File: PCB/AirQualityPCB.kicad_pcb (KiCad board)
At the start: 2 copper layers, 100 x 75 mm, 57 parts, among them J1 USB_C_Receptacle_USB2.0_16P, J10 SMA-J-P-H-ST-EM1, J2 TestPoint 5V, J3 TestPoint GND, J4 TestPoint 3.3V, U1 Regulator, U10 INIR2-ME5, U11 110-507, U12 110-303, U13 ESP32-C3-WROOM-02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

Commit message: Fixed op amp short bug
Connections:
- U7 pad 4: +3.3V -> GND
- U7 pad 8: GND -> +3.3V
- U8 pad 4: +3.3V -> GND
- U8 pad 8: GND -> +3.3V
- U9 pad 4: +3.3V -> GND
- U9 pad 8: GND -> +3.3V
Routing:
- net +3.3V: track 290.4 -> 333.6 mm
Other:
- board text added: "Air Quality Monitoring PCB MAE 5220 Designed by Robbie Leslie Cornell University School of Electrical and Computer Engineering School of Mechanical and Aerospace Engineering V1.1"
- board text removed: "Air Quality Monitoring PCB MAE 5220 Designed by Robbie Leslie Cornell University School of Electrical and Computer Engineering School of Mechanical and Aerospace Engineering"

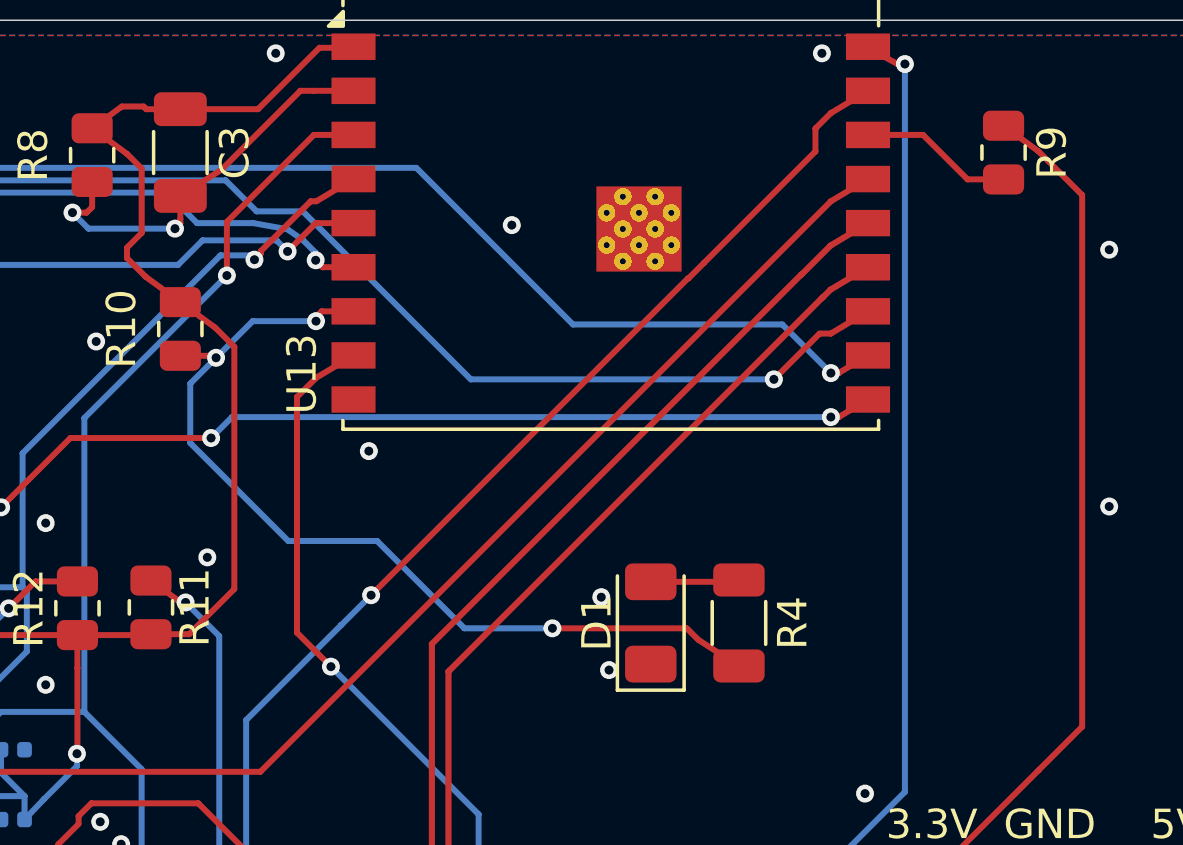
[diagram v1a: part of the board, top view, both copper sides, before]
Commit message: Swapped LED to pin 2
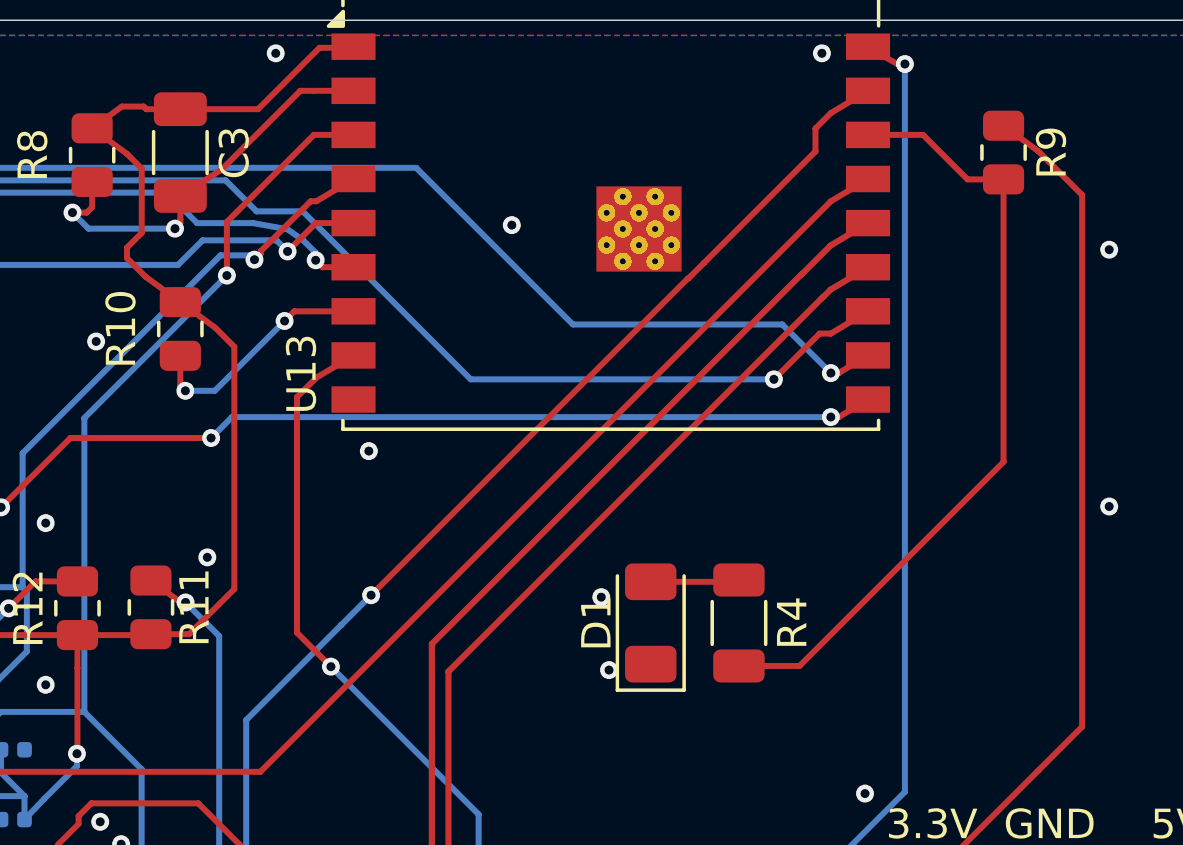
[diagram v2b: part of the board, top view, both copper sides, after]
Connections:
- R10 pad 2: /LED -> Net-(U13-IO8)
- R9 pad 2: Net-(U13-IO2) -> /LED
- U13 pad 16: Net-(U13-IO2) -> /LED
- U13 pad 7: /LED -> Net-(U13-IO8)
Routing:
- net Net-(U13-IO8): track 0.00 -> 8.28 mm, vias 0 -> 2
- net Net-(U13-IO2): track 5.24 -> 0.00 mm
- net /LED: track 31.6 -> 26.7 mm, vias 3 -> 0
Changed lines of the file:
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@@
 	(net 25 "/SDA")
 	(net 26 "Net-(U13-IO9)")
-	(net 27 "Net-(U13-IO2)")
+	(net 27 "Net-(U13-IO8)")
 	(net 28 "Net-(U5-ALERT{slash}RDY)")
 	(net 29 "Net-(U6-SDO)")
@@
 			(layers "F.Cu" "F.Mask" "F.Paste")
 			(roundrect_rratio 0.243902)
-			(net 24 "/LED")
+			(net 27 "Net-(U13-IO8)")
 			(pintype "passive")
 		)
@@
 			(layers "F.Cu" "F.Mask" "F.Paste")
 			(roundrect_rratio 0.243902)
-			(net 27 "Net-(U13-IO2)")
+			(net 24 "/LED")
 			(pintype "passive")
 		)
@@
 			(size 1.5 0.9)
 			(layers "F.Cu" "F.Mask" "F.Paste")
-			(net 24 "/LED")
+			(net 27 "Net-(U13-IO8)")
 			(pinfunction "IO8")
 			(pintype "bidirectional")
@@
 			(size 1.5 0.9)
 			(layers "F.Cu" "F.Mask" "F.Paste")
-			(net 27 "Net-(U13-IO2)")
+			(net 24 "/LED")
 			(pinfunction "IO2")
 			(pintype "bidirectional")
@@
 	)
 	(segment
-		(start 157.806025 71.578009)
-		(end 158.198926 71.97091)
-		(width 0.203403)
-		(layer "F.Cu")
-		(net 24)
-	)
-	(segment
-		(start 145.194268 61.131239)
-		(end 145.194268 60.989815)
-		(width 0.203403)
-		(layer "F.Cu")
-		(net 24)
-	)
-	(segment
-		(start 141.727007 62.308631)
-		(end 141.795009 62.376633)
-		(width 0.203403)
+		(start 161.641369 72.858631)
+		(end 168.57932 65.92068)
+		(width 0.2032)
 		(layer "F.Cu")
 		(net 24)
 	)
 	(segment
-		(start 158.198926 71.97091)
-		(end 159.579301 72.858631)
-		(width 0.203403)
+		(start 159.57932 72.858631)
+		(end 161.641369 72.858631)
+		(width 0.2032)
 		(layer "F.Cu")
 		(net 24)
 	)
 	(segment
-		(start 153.23449 71.578009)
-		(end 157.806025 71.578009)
+		(start 165.842286 54.795631)
+		(end 167.355286 56.308631)
 		(width 0.203403)
 		(layer "F.Cu")
@@
 	)
 	(segment
-		(start 145.388453 60.795631)
-		(end 146.469301 60.795631)
-		(width 0.203403)
+		(start 168.57932 65.92068)
+		(end 168.57932 56.308631)
+		(width 0.2032)
 		(layer "F.Cu")
 		(net 24)
 	)
 	(segment
-		(start 145.194268 60.989815)
-		(end 145.388453 60.795631)
+		(start 163.969301 54.795631)
+		(end 165.842286 54.795631)
 		(width 0.203403)
 		(layer "F.Cu")
@@
 	)
 	(segment
-		(start 140.579301 62.308631)
-		(end 141.727007 62.308631)
+		(start 167.355286 56.308631)
+		(end 168.579301 56.308631)
 		(width 0.203403)
 		(layer "F.Cu")
 		(net 24)
 	)
-	(via
-		(at 153.23449 71.578009)
-		(size 0.61021)
-		(drill 0.305105)
-		(layers "F.Cu" "B.Cu")
-		(net 24)
-	)
-	(via
-		(at 145.194268 61.131239)
-		(size 0.61021)
-		(drill 0.305105)
-		(layers "F.Cu" "B.Cu")
-		(net 24)
-	)
-	(via
-		(at 141.795009 62.376633)
-		(size 0.61021)
-		(drill 0.305105)
-		(layers "F.Cu" "B.Cu")
-		(net 24)
-	)
-	(segment
-		(start 140.917311 65.274479)
-		(end 140.917311 63.25433)
-		(width 0.203403)
-		(layer "B.Cu")
-		(net 24)
-	)
-	(segment
-		(start 150.241596 71.578009)
-		(end 147.272443 68.608855)
-		(width 0.203403)
-		(layer "B.Cu")
-		(net 24)
-	)
-	(segment
-		(start 153.23449 71.578009)
-		(end 150.241596 71.578009)
-		(width 0.203403)
-		(layer "B.Cu")
-		(net 24)
-	)
-	(segment
-		(start 147.272443 68.608855)
-		(end 144.251688 68.608855)
-		(width 0.203403)
-		(layer "B.Cu")
-		(net 24)
-	)
-	(segment
-		(start 140.917311 63.25433)
-		(end 141.795009 62.376633)
-		(width 0.203403)
-		(layer "B.Cu")
-		(net 24)
-	)
-	(segment
-		(start 141.795009 62.376633)
-		(end 143.040402 61.131239)
-		(width 0.203403)
-		(layer "B.Cu")
-		(net 24)
-	)
-	(segment
-		(start 144.251688 68.608855)
-		(end 140.917311 65.274479)
-		(width 0.203403)
-		(layer "B.Cu")
-		(net 24)
-	)
-	(segment
-		(start 143.040402 61.131239)
-		(end 145.194268 61.131239)
-		(width 0.203403)
-		(layer "B.Cu")
-		(net 24)
-	)
 	(segment
 		(start 134.07932 82.858631)
@@
 	)
 	(segment
-		(start 165.842286 54.795631)
-		(end 167.355286 56.308631)
-		(width 0.203403)
+		(start 140.57932 63.32932)
+		(end 140.75 63.5)
+		(width 0.2032)
 		(layer "F.Cu")
 		(net 27)
 	)
 	(segment
-		(start 163.969301 54.795631)
-		(end 165.842286 54.795631)
-		(width 0.203403)
+		(start 140.57932 62.308631)
+		(end 140.57932 63.32932)
+		(width 0.2032)
 		(layer "F.Cu")
 		(net 27)
 	)
 	(segment
-		(start 167.355286 56.308631)
-		(end 168.579301 56.308631)
-		(width 0.203403)
+		(start 144.453869 60.796131)
+		(end 144.125 61.125)
+		(width 0.2032)
 		(layer "F.Cu")
 		(net 27)
 	)
+	(segment
+		(start 144.125 61.125)
+		(end 144 61.25)
+		(width 0.2032)
+		(layer "F.Cu")
+		(net 27)
+	)
+	(segment
+		(start 146.46932 60.796131)
+		(end 144.453869 60.796131)
+		(width 0.2032)
+		(layer "F.Cu")
+		(net 27)
+	)
+	(via
+		(at 144.125 61.125)
+		(size 0.6096)
+		(drill 0.3048)
+		(layers "F.Cu" "B.Cu")
+		(net 27)
+	)
+	(via
+		(at 140.75 63.5)
+		(size 0.6096)
+		(drill 0.3048)
+		(layers "F.Cu" "B.Cu")
+		(net 27)
+	)
+	(segment
+		(start 144.125 61.125)
+		(end 141.75 63.5)
+		(width 0.2032)
+		(layer "B.Cu")
+		(net 27)
+	)
+	(segment
+		(start 141.75 63.5)
+		(end 140.75 63.5)
+		(width 0.2032)
+		(layer "B.Cu")
+		(net 27)
+	)

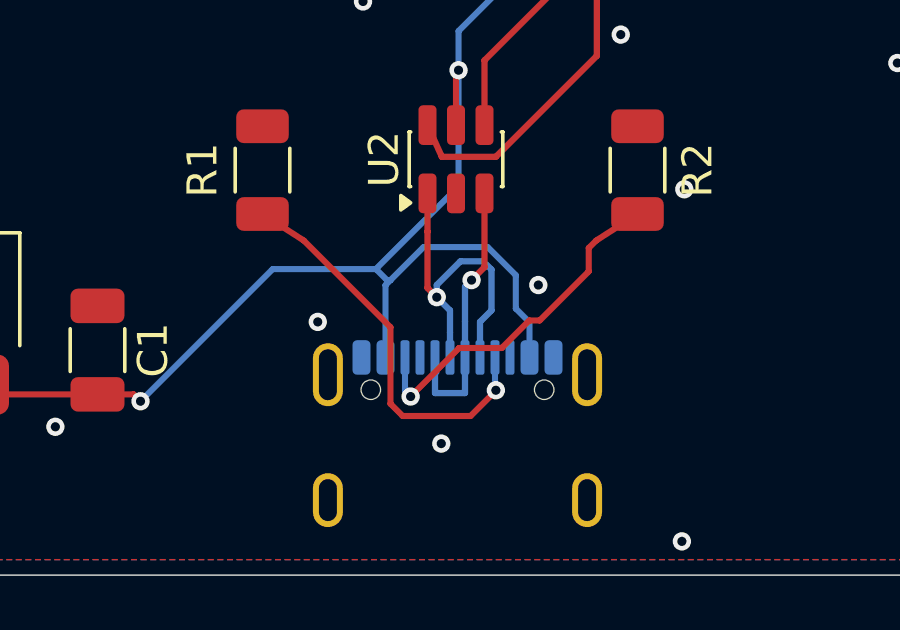
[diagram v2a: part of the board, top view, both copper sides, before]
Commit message: Swapped USB CC resistors
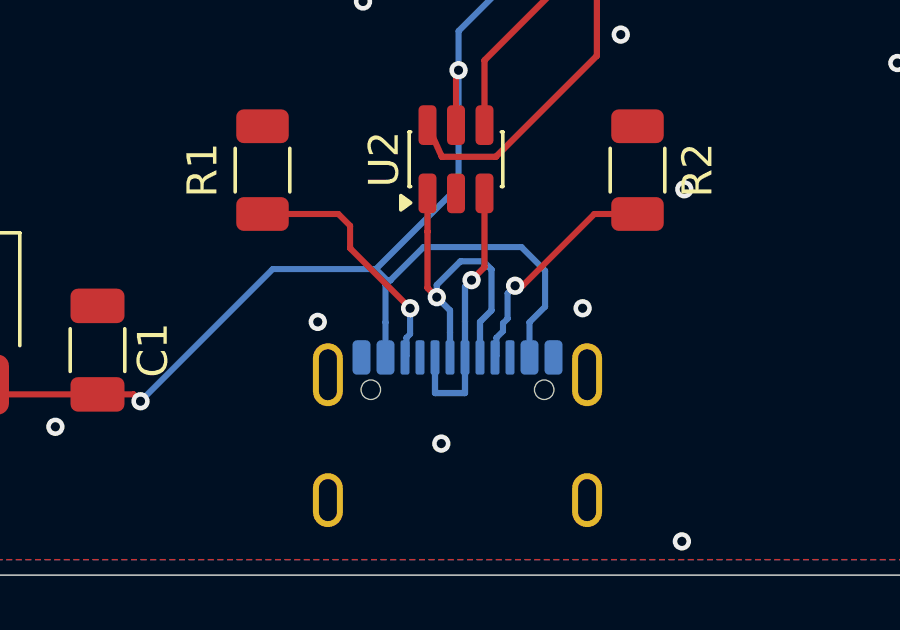
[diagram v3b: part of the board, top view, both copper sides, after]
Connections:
- R1 pad 2: Net-(J1-CC1) -> Net-(J1-CC2)
- R2 pad 2: Net-(J1-CC2) -> Net-(J1-CC1)
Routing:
- net Net-(J1-CC1): track 13.4 -> 7.74 mm
- net Net-(J1-CC2): track 11.8 -> 8.37 mm
- net VBUS: track 89.8 -> 90.9 mm
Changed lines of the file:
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@@
 	(title_block
 		(title "Air Quality PCB")
-		(date "2026-04-12")
+		(date "2026-04-13")
 		(rev "v1.1")
 		(company "Cornell University")
@@
 			(layers "F.Cu" "F.Mask" "F.Paste")
 			(roundrect_rratio 0.222222)
-			(net 17 "Net-(J1-CC2)")
+			(net 21 "Net-(J1-CC1)")
 			(pintype "passive")
 		)
@@
 			(layers "F.Cu" "F.Mask" "F.Paste")
 			(roundrect_rratio 0.222222)
-			(net 21 "Net-(J1-CC1)")
+			(net 17 "Net-(J1-CC2)")
 			(pintype "passive")
 		)
@@
 	)
 	(via
-		(at 135.773774 116.226423)
+		(at 137.25 117)
 		(size 0.61021)
 		(drill 0.305105)
@@
 	(segment
 		(start 135.479301 117.467149)
-		(end 135.023121 117.010969)
+		(end 136 116.94645)
 		(width 0.203403)
 		(layer "B.Cu")
@@
 	)
 	(segment
-		(start 134.083183 114.961082)
-		(end 131.947332 114.961082)
+		(start 136 115.75)
+		(end 135.211082 114.961082)
 		(width 0.203403)
 		(layer "B.Cu")
@@
 	)
 	(segment
-		(start 135.023121 115.901019)
-		(end 134.083183 114.961082)
-		(width 0.203403)
-		(layer "B.Cu")
-		(net 2)
-	)
-	(segment
 		(start 130.679301 116.229113)
 		(end 130.679301 117.467149)
@@
 	)
 	(segment
-		(start 131.947332 114.961082)
-		(end 130.848078 116.060336)
+		(start 130.848078 116.060336)
+		(end 130.679301 116.229113)
 		(width 0.203403)
 		(layer "B.Cu")
@@
 	)
 	(segment
-		(start 130.848078 116.060336)
-		(end 130.679301 116.229113)
+		(start 133.11458 112.939512)
+		(end 133.11458 109.066198)
 		(width 0.203403)
 		(layer "B.Cu")
@@
 	)
 	(segment
-		(start 133.11458 112.939512)
-		(end 133.11458 109.066198)
+		(start 135.211082 114.961082)
+		(end 131.947332 114.961082)
 		(width 0.203403)
 		(layer "B.Cu")
@@
 	)
 	(segment
-		(start 135.023121 117.010969)
-		(end 135.023121 115.901019)
+		(start 135.479301 118.641131)
+		(end 135.479301 117.467149)
 		(width 0.203403)
 		(layer "B.Cu")
@@
 	)
 	(segment
-		(start 142.135633 101.061384)
-		(end 139.813917 101.061384)
+		(start 136 116.94645)
+		(end 136 115.75)
 		(width 0.203403)
 		(layer "B.Cu")
@@
 	)
 	(segment
-		(start 130.725595 116.060336)
-		(end 130.848078 116.060336)
+		(start 142.135633 101.061384)
+		(end 139.813917 101.061384)
 		(width 0.203403)
 		(layer "B.Cu")
@@
 	)
 	(segment
-		(start 135.479301 118.641131)
-		(end 135.479301 117.467149)
+		(start 130.725595 116.060336)
+		(end 130.848078 116.060336)
 		(width 0.203403)
 		(layer "B.Cu")
@@
 	)
 	(segment
+		(start 131.947332 114.961082)
+		(end 130.848078 116.060336)
+		(width 0.203403)
+		(layer "B.Cu")
+		(net 2)
+	)
+	(segment
 		(start 130.679301 117.467149)
 		(end 130.679301 118.641131)
@@
 	)
 	(segment
-		(start 133.133566 118.325096)
-		(end 134.554057 118.325096)
+		(start 129.108631 113.858631)
+		(end 126.57932 113.858631)
 		(width 0.203403)
 		(layer "F.Cu")
@@
 	)
 	(segment
-		(start 137.45351 114.991768)
-		(end 137.698926 114.746352)
+		(start 129.5 115)
+		(end 129.5 114.25)
 		(width 0.203403)
 		(layer "F.Cu")
@@
 	)
 	(segment
-		(start 135.818381 117.407843)
-		(end 137.45351 115.772714)
+		(start 131.5 117)
+		(end 129.5 115)
 		(width 0.203403)
 		(layer "F.Cu")
@@
 	)
 	(segment
-		(start 137.45351 115.772714)
-		(end 137.45351 114.991768)
+		(start 129.5 114.25)
+		(end 129.108631 113.858631)
 		(width 0.203403)
 		(layer "F.Cu")
 		(net 17)
 	)
-	(segment
-		(start 131.516481 119.942182)
-		(end 133.133566 118.325096)
-		(width 0.203403)
-		(layer "F.Cu")
-		(net 17)
-	)
-	(segment
-		(start 135.471311 117.407843)
-		(end 135.818381 117.407843)
-		(width 0.203403)
-		(layer "F.Cu")
+	(via
+		(at 131.5 117)
+		(size 0.61021)
+		(drill 0.305105)
+		(layers "F.Cu" "B.Cu")
 		(net 17)
 	)
 	(segment
-		(start 137.698926 114.746352)
-		(end 139.079301 113.858631)
+		(start 131.5 117.860635)
+		(end 131.377618 117.983017)
 		(width 0.203403)
-		(layer "F.Cu")
+		(layer "B.Cu")
 		(net 17)
 	)
 	(segment
-		(start 134.554057 118.325096)
-		(end 135.471311 117.407843)
+		(start 131.5 117)
+		(end 131.5 117.860635)
 		(width 0.203403)
-		(layer "F.Cu")
-		(net 17)
-	)
-	(via
-		(at 131.516481 119.942182)
-		(size 0.61021)
-		(drill 0.305105)
-		(layers "F.Cu" "B.Cu")
+		(layer "B.Cu")
 		(net 17)
 	)
 	(segment
-		(start 131.329301 119.755002)
-		(end 131.516481 119.942182)
+		(start 131.377618 118.592814)
+		(end 131.329301 118.641131)
 		(width 0.203403)
 		(layer "B.Cu")
@@
 	)
 	(segment
-		(start 131.329301 118.641131)
-		(end 131.329301 119.755002)
+		(start 131.377618 117.983017)
+		(end 131.377618 118.592814)
 		(width 0.203403)
 		(layer "B.Cu")
@@
 	)
 	(segment
-		(start 130.845024 120.185836)
-		(end 130.845024 117.631701)
+		(start 135.25 116.25)
+		(end 137.641369 113.858631)
 		(width 0.203403)
 		(layer "F.Cu")
@@
 	)
 	(segment
-		(start 134.261574 119.829739)
-		(end 134.261574 119.845476)
+		(start 135 116.25)
+		(end 135.25 116.25)
 		(width 0.203403)
 		(layer "F.Cu")
@@
 	)
 	(segment
-		(start 134.357964 119.733349)
-		(end 134.261574 119.829739)
+		(start 137.641369 113.858631)
+		(end 139.07932 113.858631)
 		(width 0.203403)
 		(layer "F.Cu")
 		(net 21)
 	)
-	(segment
-		(start 131.251143 120.591955)
-		(end 130.845024 120.185836)
-		(width 0.203403)
-		(layer "F.Cu")
+	(via
+		(at 135 116.25)
+		(size 0.61021)
+		(drill 0.305105)
+		(layers "F.Cu" "B.Cu")
 		(net 21)
 	)
 	(segment
-		(start 133.515095 120.591955)
-		(end 131.251143 120.591955)
+		(start 134.75 117.346206)
+		(end 134.596206 117.5)
 		(width 0.203403)
-		(layer "F.Cu")
+		(layer "B.Cu")
 		(net 21)
 	)
 	(segment
-		(start 127.959675 114.746352)
-		(end 126.579301 113.858631)
+		(start 134.596206 117.5)
+		(end 134.596206 117.764429)
 		(width 0.203403)
-		(layer "F.Cu")
+		(layer "B.Cu")
 		(net 21)
 	)
 	(segment
-		(start 134.261574 119.845476)
-		(end 133.515095 120.591955)
+		(start 134.75 116.5)
+		(end 134.75 117.346206)
 		(width 0.203403)
-		(layer "F.Cu")
+		(layer "B.Cu")
 		(net 21)
 	)
 	(segment
-		(start 130.845024 117.631701)
-		(end 127.959675 114.746352)
+		(start 134.596206 117.764429)
+		(end 134.377618 117.983017)
 		(width 0.203403)
-		(layer "F.Cu")
-		(net 21)
-	)
-	(via
-		(at 134.357964 119.733349)
-		(size 0.61021)
-		(drill 0.305105)
-		(layers "F.Cu" "B.Cu")
+		(layer "B.Cu")
 		(net 21)
 	)
 	(segment
-		(start 134.357964 119.733349)
-		(end 134.329301 119.704685)
+		(start 134.377618 117.983017)
+		(end 134.377618 118.592814)
 		(width 0.203403)
 		(layer "B.Cu")
@@
 	)
 	(segment
-		(start 134.329301 119.704685)
-		(end 134.329301 119.623946)
+		(start 134.377618 118.592814)
+		(end 134.329301 118.641131)
 		(width 0.203403)
 		(layer "B.Cu")
@@
 	)
 	(segment
-		(start 134.329301 119.623946)
-		(end 134.329301 118.641131)
+		(start 135 116.25)
+		(end 134.75 116.5)
 		(width 0.203403)
 		(layer "B.Cu")
